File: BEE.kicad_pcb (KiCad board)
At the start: 2 copper layers, 77.5 x 81.5 mm, 74 parts, among them J1 RPI1_header, J10 Conn_01x02, J11 Conn_01x02, J12 Conn_01x02, J13 Conn_01x06, J14 Conn_01x03, J15 Conn_02x10_Odd_Even, J16 Conn_01x08, J17 Conn_01x03, J18 Conn_01x03, J19 Conn_01x03, J2 Conn_02x05_Odd_Even, J20 Conn_01x10, J3 Conn_01x03, J4 Conn_01x06, J5 Conn_02x10_Odd_Even, J6 Conn_01x06, J7 Conn_02x10_Odd_Even, J8 Conn_01x08, J9 Conn_01x02, SW1 SW_Push, SW2 SW_Push, SW3 SW_Push, U1 MCP3008, U2 MCP4911, U3 Dip_10xsp3t, U4 Dip_10xsp3t, U5 74AHC595, U6 Display_7Segments

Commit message: ucm logo and project moved
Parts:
- moved LOGO3 3.02 mm to (149.0, 100.2)
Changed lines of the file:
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@@
   )
   (module BEElib:UCMLogo_169_169 (layer B.Cu)
-    (at 149.0472 97.1804 180)
+    (at 148.9964 100.203 180)
     (fp_text reference LOGO3 (at 0 0 180) (layer B.SilkS) hide
       (effects (font (size 1.524 1.524) (thickness 0.3)) (justify mirror))
@@
     (effects (font (size 0.75 0.75) (thickness 0.15)))
   )
-  (gr_text "https://github.com/tenllado/bee\nrev 2.0\n" (at 149.0472 106.9594) (layer B.SilkS)
+  (gr_text "https://github.com/tenllado/bee\nrev 2.0\n" (at 149.0218 109.6518) (layer B.SilkS)
     (effects (font (size 1 1) (thickness 0.15)) (justify mirror))
   )

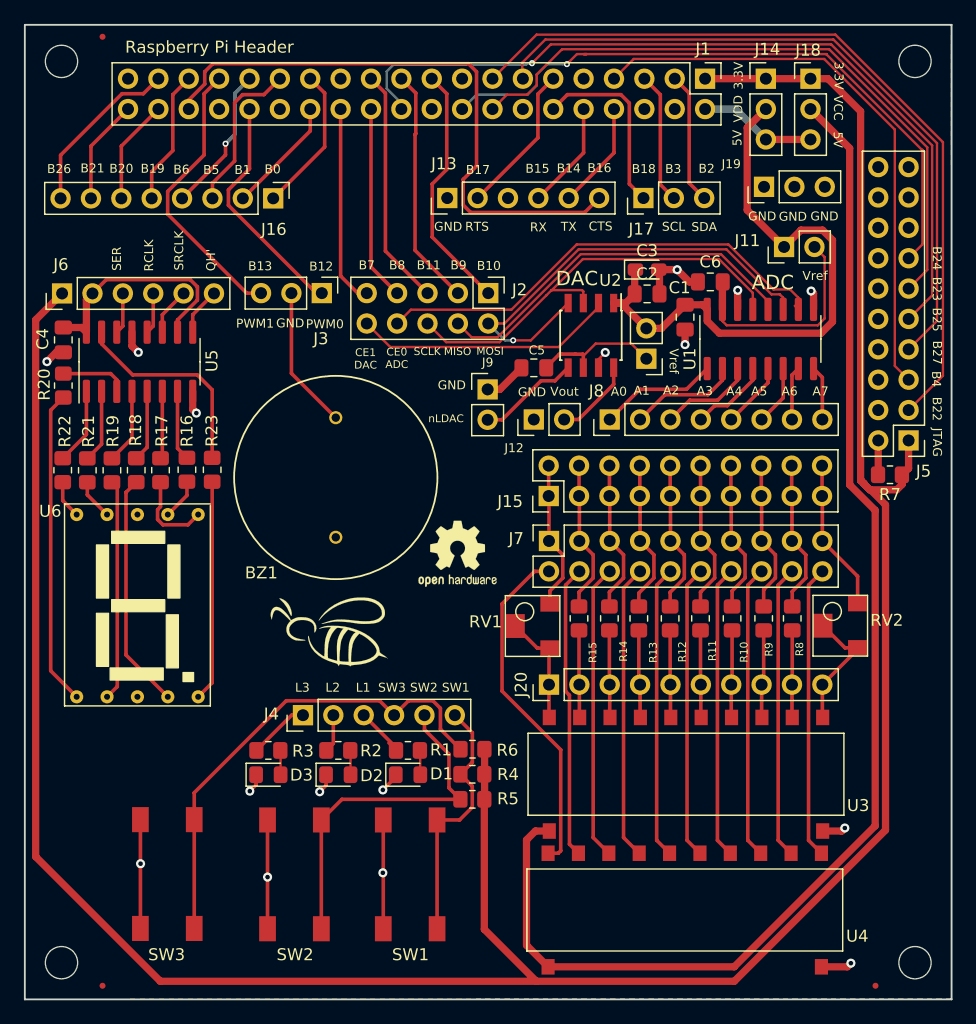
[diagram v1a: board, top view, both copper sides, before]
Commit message: RGB Led and J17 adaptation to pimoroni breakouts
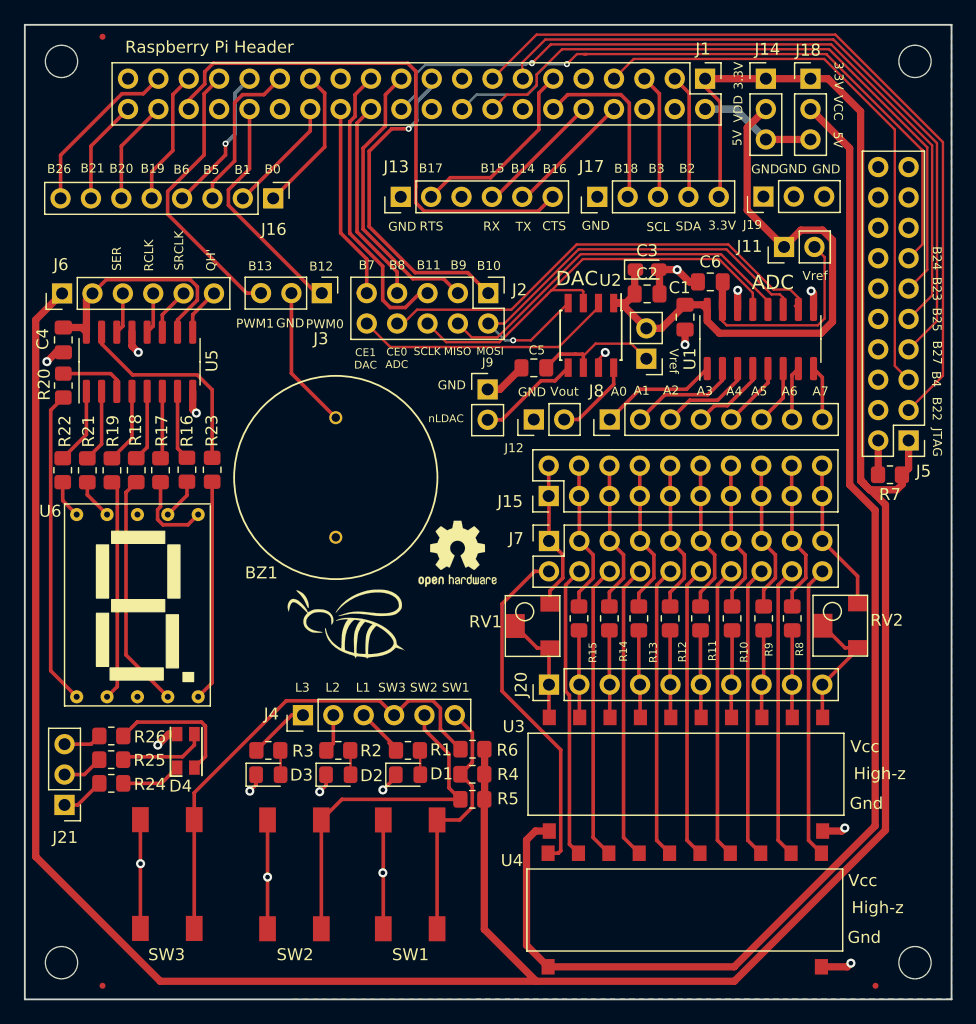
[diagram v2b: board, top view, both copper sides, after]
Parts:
- added D4: LED_RCGB, BEElib:LED_RCGB, F.Cu at (107.8, 94.2)
- added J21: Conn_01x03, Connector_PinHeader_2.54mm:PinHeader_1x03_P2.54mm_Vertical, F.Cu at (97.7, 98.8)
- added R24: 280, Resistor_SMD:R_0805_2012Metric_Pad1.20x1.40mm_HandSolder, F.Cu at (101.6, 97.0)
- added R25: 100, Resistor_SMD:R_0805_2012Metric_Pad1.20x1.40mm_HandSolder, F.Cu at (101.6, 95.0)
- added R26: 100, Resistor_SMD:R_0805_2012Metric_Pad1.20x1.40mm_HandSolder, F.Cu at (101.6, 93.0)
- J17: value Conn_01x03 -> Conn_01x05; footprint Connector_PinHeader_2.54mm:PinHeader_1x03_P2.54mm_Vertical -> Connector_PinHeader_2.54mm:PinHeader_1x05_P2.54mm_Vertical
- RV1, RV2: value R_POT -> 100k
- moved J13 3.89 mm to (125.8, 47.9)
- moved J17 3.86 mm to (142.3, 47.9)
- moved LOGO2 1.57 mm to (121.4, 83.6)
- moved J19 0.81 mm to (156.2, 47.9)
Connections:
- J17 pad 1: /BCM18 -> GND
- J17 pad 2: /BCM3_SCL -> /BCM18
- J17 pad 3: /BCM2_SDA -> /BCM3_SCL
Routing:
- net Net-(D4-Pad4): track 0.00 -> 11.3 mm
- net +3V3: track 233.0 -> 243.4 mm
- net Net-(D4-Pad3): track 0.00 -> 7.37 mm
- net /BCM10_MOSI: track 20.9 -> 27.6 mm, vias 0 -> 1
- net /BCM16_CTS: track 50.7 -> 45.1 mm
- net Net-(D4-Pad1): track 0.00 -> 5.04 mm
- net /BCM11_SCLK: track 19.9 -> 24.9 mm
- net /BCM9_MISO: track 19.9 -> 24.0 mm
- net Net-(J21-Pad1): track 0.00 -> 3.66 mm
- net /BCM17_RTS: track 12.6 -> 16.1 mm
- net Net-(J21-Pad2): track 0.00 -> 3.42 mm
- net Net-(J21-Pad3): track 0.00 -> 3.20 mm
- net /BCM25_TCK: track 69.0 -> 66.9 mm
- net GND: track 57.9 -> 59.9 mm, vias 16 -> 17
- net /BCM14_TX: track 9.01 -> 10.7 mm
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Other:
- board text added: "Gnd"
- board text added: "High-z"
- board text added: "Vcc"

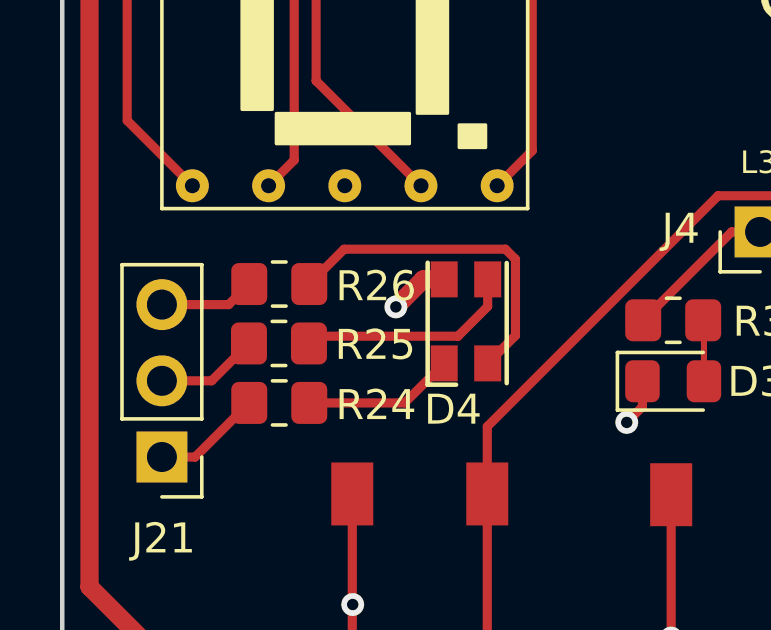
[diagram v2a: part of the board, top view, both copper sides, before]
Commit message: small rerouting of rgb led module
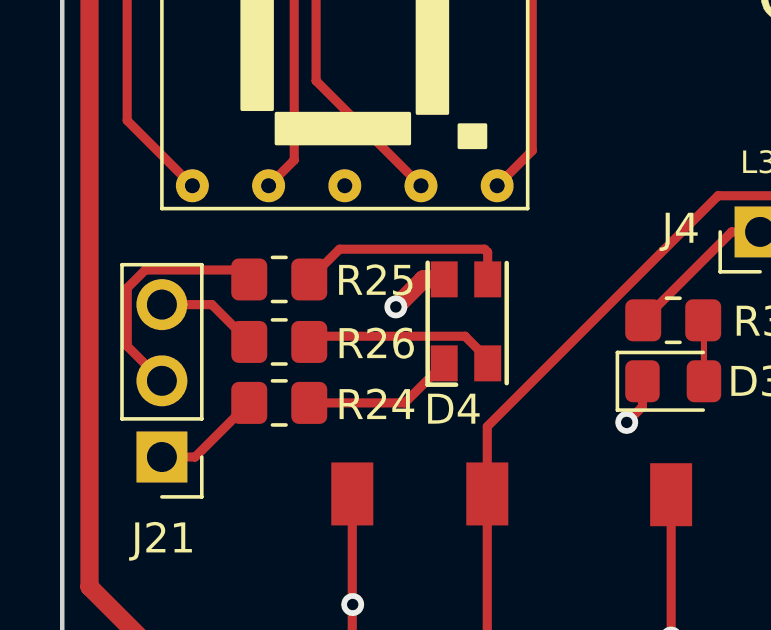
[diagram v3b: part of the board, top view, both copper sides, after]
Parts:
- moved R25 2.13 mm to (101.6, 92.8)
- moved R26 1.93 mm to (101.6, 94.9)
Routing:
- net Net-(D4-Pad4): track 11.3 -> 6.49 mm
- net Net-(J21-Pad2): track 3.42 -> 8.02 mm

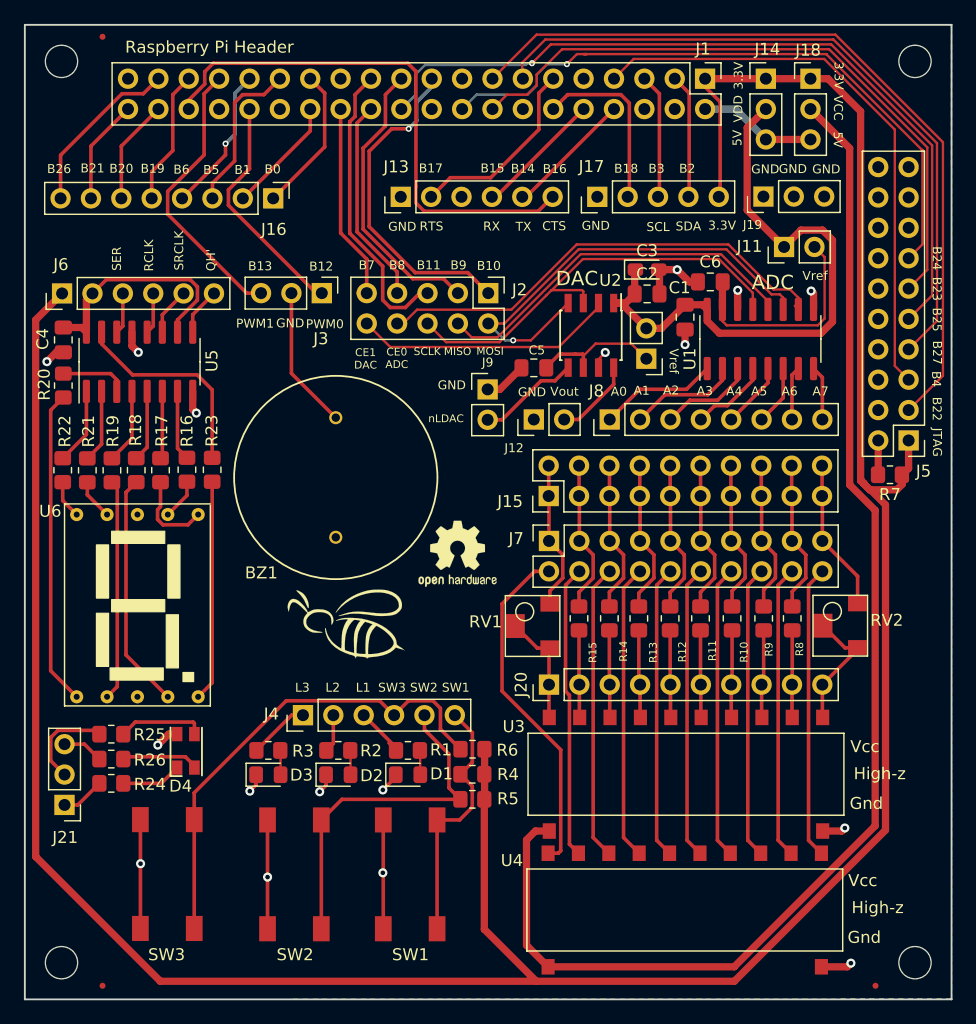
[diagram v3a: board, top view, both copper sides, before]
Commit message: Migration to kicad 6.0
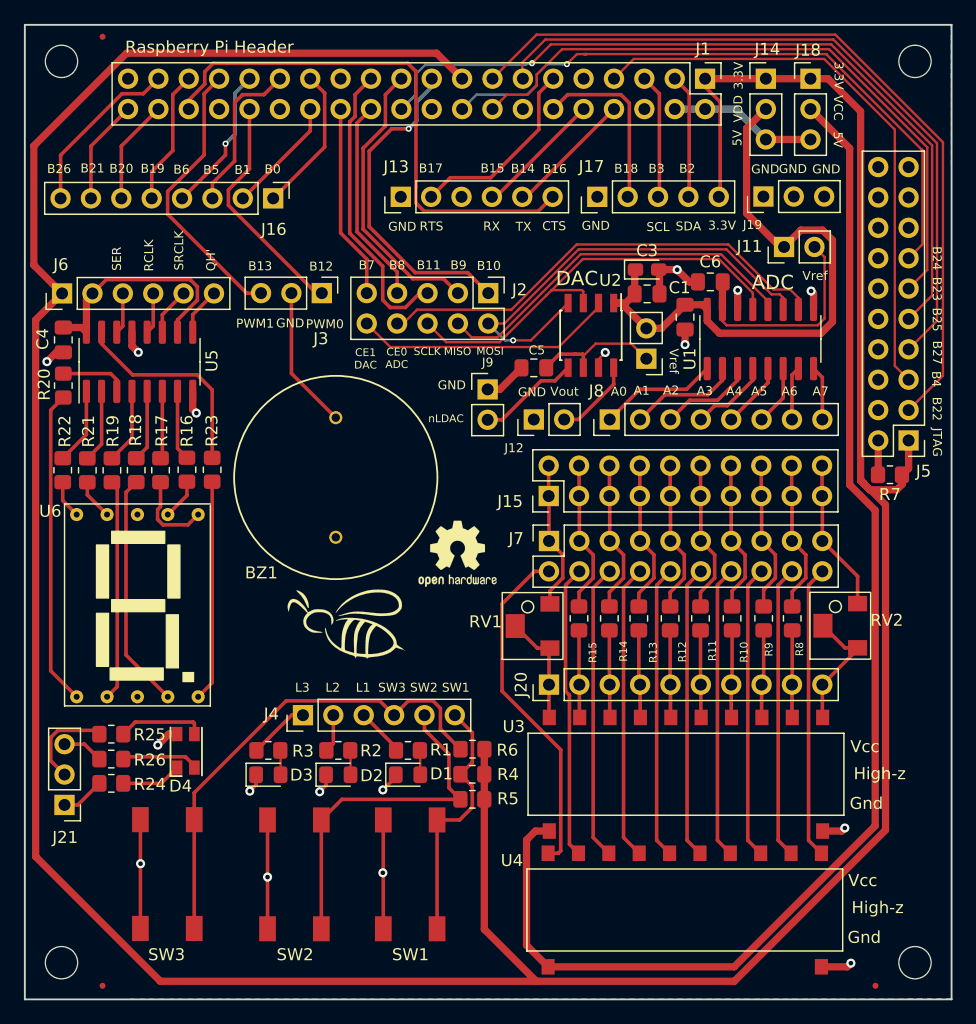
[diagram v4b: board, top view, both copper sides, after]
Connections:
- J1 pad 17: (no net) -> +3V3
- J1 pad 4: (no net) -> +5V
- J13 pad 3: (no net) -> unconnected-(J13-Pad3)
- J5 pad 15: (no net) -> unconnected-(J5-Pad15)
- J5 pad 17: (no net) -> unconnected-(J5-Pad17)
- J5 pad 19: (no net) -> unconnected-(J5-Pad19)
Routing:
- net +3V3: track 243.4 -> 296.6 mm
- net +5V: track 9.97 -> 12.4 mm
- net /BCM7_CE1: track 17.7 -> 16.3 mm
- net /L1: track 4.95 -> 4.06 mm
- net /BCM22_TRST: track 67.0 -> 66.5 mm
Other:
- net class Default removed
- net class Power removed
- net class signal removed

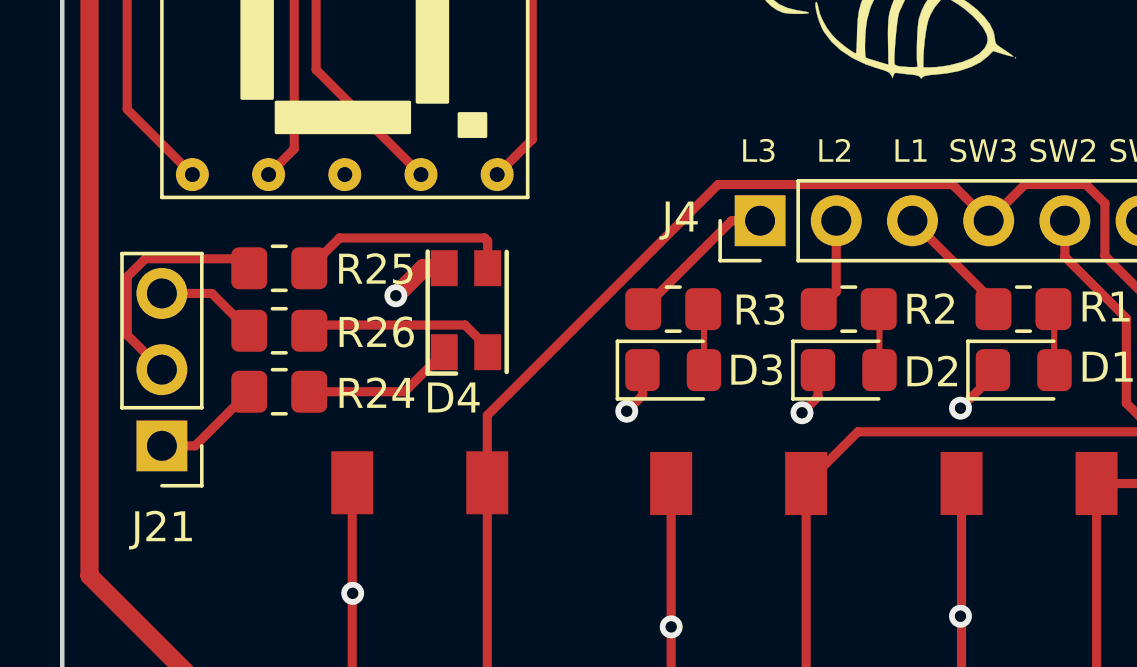
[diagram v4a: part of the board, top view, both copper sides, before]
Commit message: changed RGB led by a bigger 5050 one
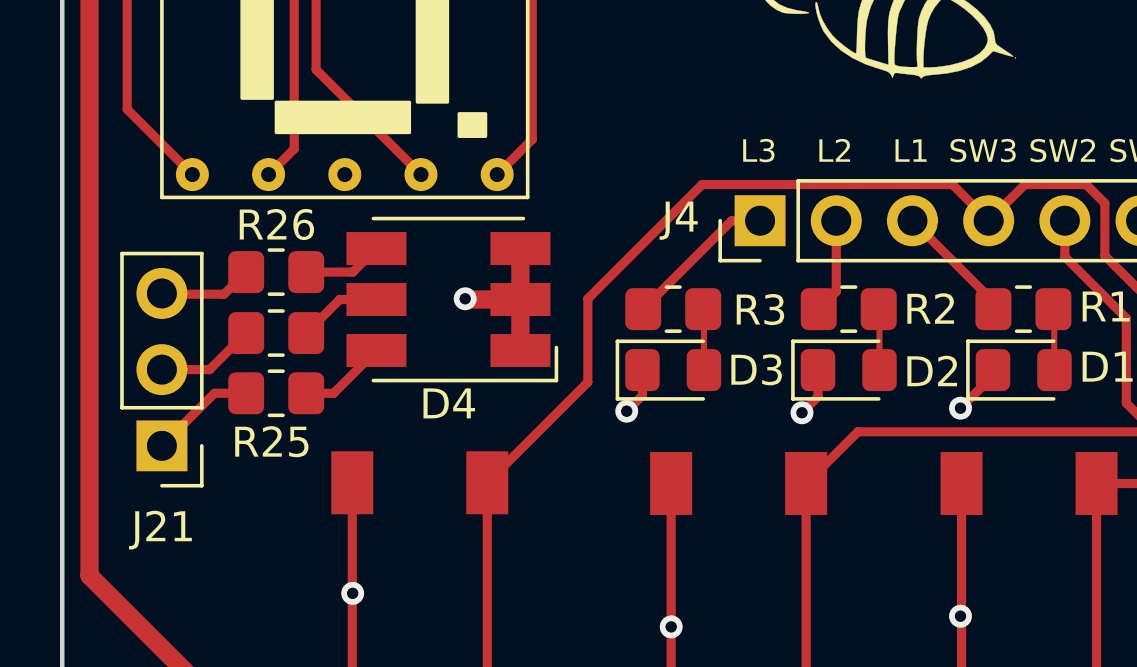
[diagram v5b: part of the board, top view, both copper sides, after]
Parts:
- D4: value LED_RCGB -> LED_RGB; footprint BEElib:LED_RCGB -> LED_SMD:LED_RGB_5050-6
- moved R25 4.17 mm to (101.5, 97.0)
- moved R24 1.96 mm to (101.5, 95.0)
- moved R26 1.96 mm to (101.5, 93.0)
- moved D4 0.68 mm to (107.3, 93.9), turned to 180 degrees
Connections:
- D4 pad 1: Net-(D4-Pad1) -> GND
- D4 pad 3: Net-(D4-Pad3) -> GND
- R24 pad 1: Net-(J21-Pad1) -> Net-(J21-Pad2)
- R24 pad 2: Net-(D4-Pad1) -> Net-(D4-Pad5)
- R25 pad 1: Net-(J21-Pad2) -> Net-(J21-Pad1)
- R25 pad 2: Net-(D4-Pad3) -> Net-(D4-Pad6)
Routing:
- net Net-(D4-Pad3): track 7.31 -> 0.00 mm
- net Net-(D4-Pad1): track 5.04 -> 0.00 mm
- net Net-(J21-Pad2): track 8.02 -> 3.32 mm
- net Net-(R26-Pad2): track 6.49 -> 2.67 mm
- net GND: track 59.9 -> 63.4 mm
- net Net-(D4-Pad6): track 0.00 -> 2.93 mm
- net Net-(D4-Pad5): track 0.00 -> 2.80 mm

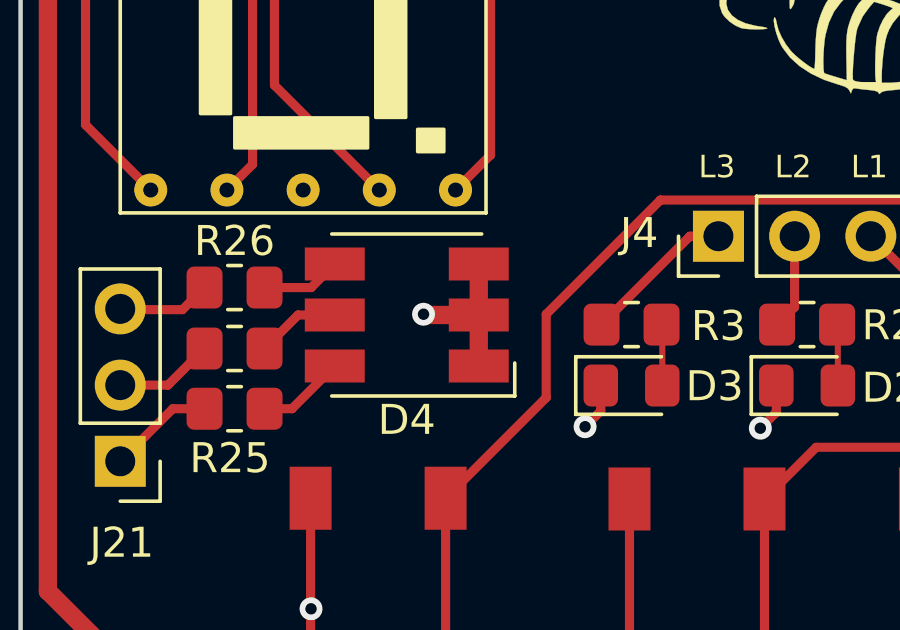
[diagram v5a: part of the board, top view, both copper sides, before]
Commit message: D4 pin numbering adjusted on schematic and footprint, according to datasheet
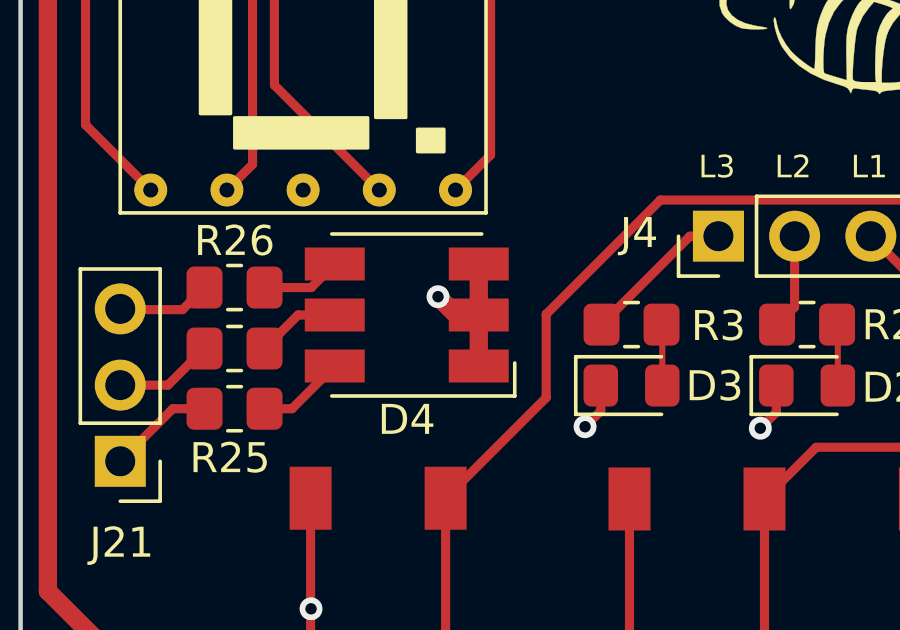
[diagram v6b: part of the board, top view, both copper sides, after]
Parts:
- D4: footprint LED_SMD:LED_RGB_5050-6 -> BEElib:LED_RGB_5050-6
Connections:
- D4 pad 2: GND -> Net-(D4-Pad2)
- D4 pad 4: Net-(R26-Pad2) -> Net-(D4-Pad4)
- D4 pad 5: Net-(D4-Pad5) -> GND
- D4 pad 6: Net-(D4-Pad6) -> Net-(R26-Pad2)
- R24 pad 2: Net-(D4-Pad5) -> Net-(D4-Pad4)
- R25 pad 2: Net-(D4-Pad6) -> Net-(D4-Pad2)
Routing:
- net Net-(D4-Pad6): track 2.93 -> 0.00 mm
- net Net-(D4-Pad2): track 0.00 -> 2.93 mm
- net Net-(D4-Pad5): track 2.80 -> 0.00 mm
- net Net-(D4-Pad4): track 0.00 -> 2.80 mm
